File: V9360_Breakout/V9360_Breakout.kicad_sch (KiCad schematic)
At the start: 1 part

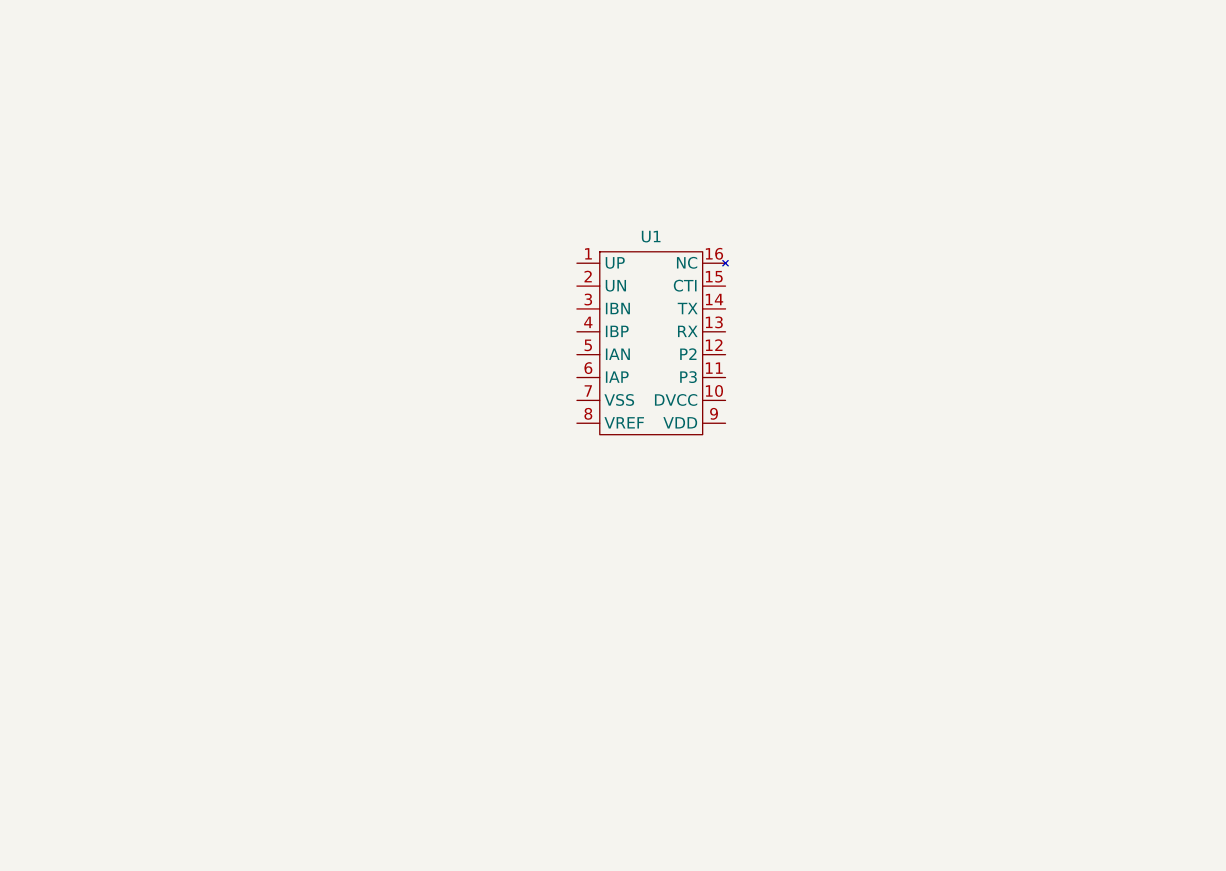
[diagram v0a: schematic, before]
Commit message: Add routing and filters
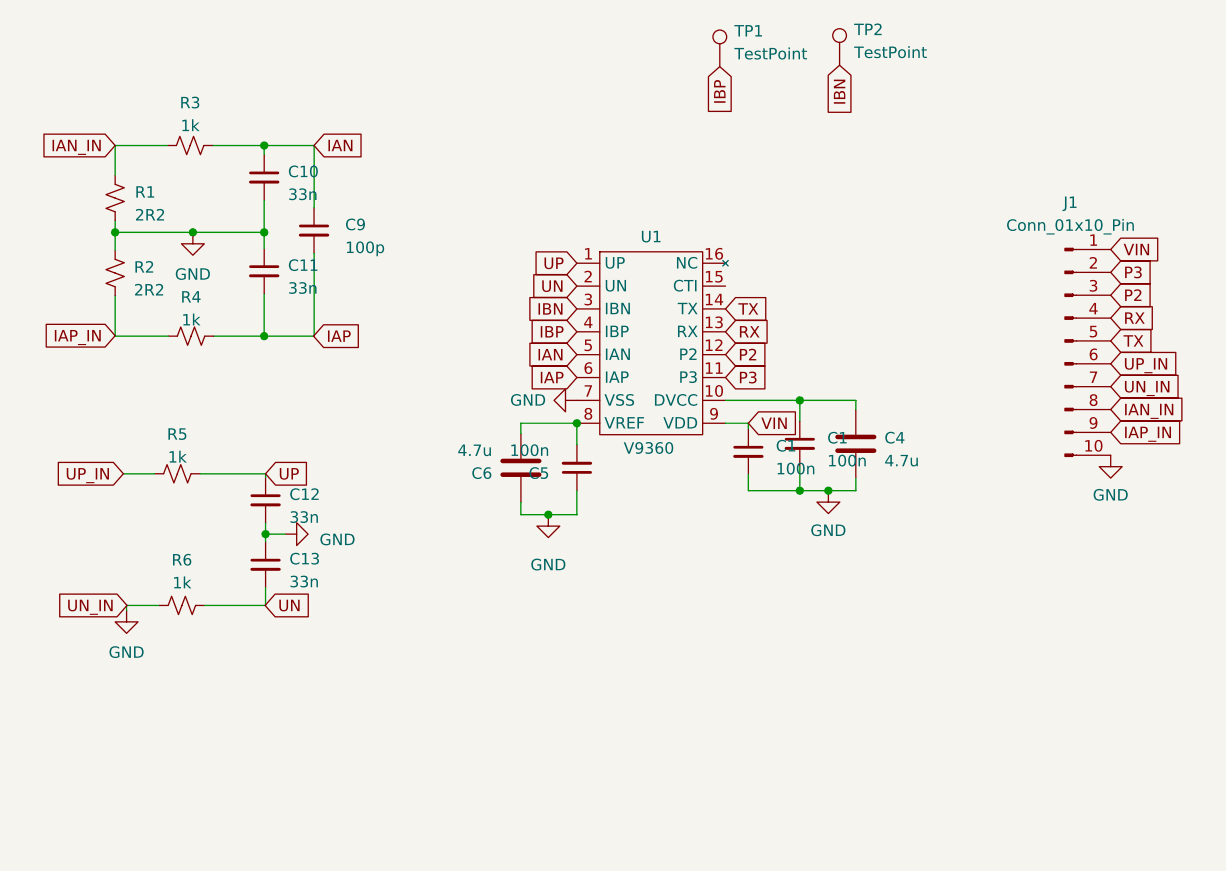
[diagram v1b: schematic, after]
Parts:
- added C1 (x2), C5: 100n, Capacitor_SMD:C_0603_1608Metric, symbol Device:C_Small
- added C10, C11, C12, C13: 33n, Capacitor_SMD:C_0603_1608Metric, symbol Device:C_Small
- added C4, C6: 4.7u, Capacitor_SMD:C_0805_2012Metric, symbol Device:C
- added C9: 100p, Capacitor_SMD:C_0603_1608Metric, symbol Device:C_Small
- added J1: Conn_01x10_Pin, Connector_PinHeader_2.54mm:PinHeader_1x10_P2.54mm_Vertical, symbol Connector:Conn_01x10_Pin
- added R1, R2: 2R2, Resistor_SMD:R_0603_1608Metric, symbol Device:R_Small_US
- added R3, R4, R5, R6: 1k, Resistor_SMD:R_0603_1608Metric, symbol Device:R_Small_US
- added TP1, TP2: TestPoint, TestPoint:TestPoint_Pad_1.5x1.5mm, symbol Connector:TestPoint
- U1: value ~ -> V9360
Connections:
- net UP: now reaches U1.1 (UP)
- net UP: now also C12.1, R5.2
- net at U1.10 (DVCC): now also C1.1, C4.1
- net P3: now reaches U1.11 (P3)
- net P3: now also J1.2 (Pin_2)
- net P2: now reaches U1.12 (P2)
- net P2: now also J1.3 (Pin_3)
- net RX: now reaches U1.13 (RX)
- net RX: now also J1.4 (Pin_4)
- net TX: now reaches U1.14 (TX)
- net TX: now also J1.5 (Pin_5)
- net UN: now reaches U1.2 (UN)
- net UN: now also C13.2, R6.2
- net IBN: now reaches U1.3 (IBN)
- net IBN: now also TP2.1
- net IBP: now reaches U1.4 (IBP)
- net IBP: now also TP1.1
- net IAN: now reaches U1.5 (IAN)
- net IAN: now also C10.1, C9.1, R3.2
- net IAP: now reaches U1.6 (IAP)
- net IAP: now also C11.2, C9.2, R4.2
- net GND: now reaches U1.7 (VSS)
- net GND: now also C1.2, C1.2, C10.2, C11.1, C12.2, C13.1, C4.2, C5.1, C6.1, J1.10 (Pin_10), J1.7 (Pin_7), R1.2, R2.1, R6.1
- net at U1.8 (VREF): now also C5.2, C6.2
- net VIN: now reaches U1.9 (VDD)
- net VIN: now also C1.1, J1.1 (Pin_1)
- new net IAN_IN: J1.8 (Pin_8), R1.1, R3.1
- new net IAP_IN: J1.9 (Pin_9), R2.2, R4.1
- new net UP_IN: J1.6 (Pin_6), R5.1

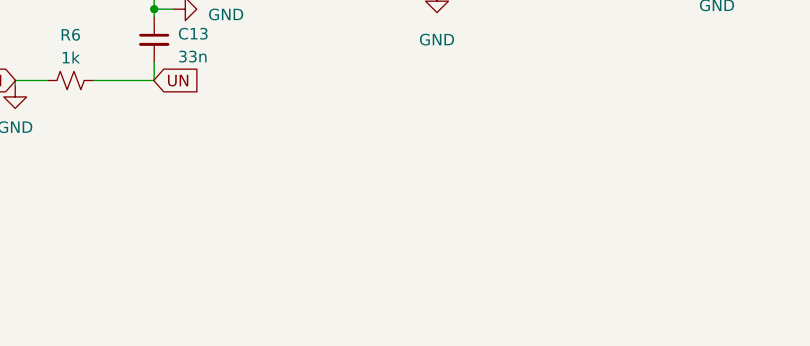
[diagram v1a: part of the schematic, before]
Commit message: Add silk screen refinements
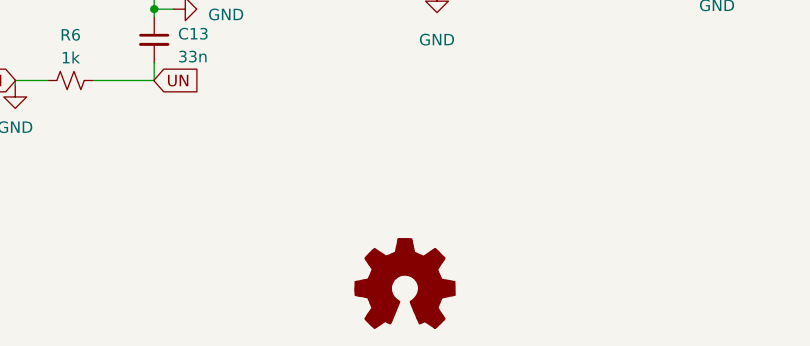
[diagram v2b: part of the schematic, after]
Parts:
- added SYM1: Logo_Open_Hardware_Small, Symbol:OSHW-Logo2_9.8x8mm_SilkScreen, symbol Graphic:Logo_Open_Hardware_Small
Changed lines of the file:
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@@
+    )
+  )
+  (symbol (lib_id "Graphic:Logo_Open_Hardware_Small") (at 125.603 147.955 0) (unit 1)
+    (in_bom no) (on_board yes) (dnp no) (fields_autoplaced)
+    (property "Reference" "SYM1" (at 125.603 140.97 0)
+      (effects (font (size 1.27 1.27)) hide)
+    )
+    (property "Value" "Logo_Open_Hardware_Small" (at 125.603 153.67 0)
+      (effects (font (size 1.27 1.27)) hide)
+    )
+    (property "Footprint" "Symbol:OSHW-Logo2_9.8x8mm_SilkScreen" (at 125.603 147.955 0)
+      (effects (font (size 1.27 1.27)) hide)
+    )
+    (property "Datasheet" "~" (at 125.603 147.955 0)
+      (effects (font (size 1.27 1.27)) hide)
+    )
+    (property "Sim.Enable" "0" (at 125.603 147.955 0)
+      (effects (font (size 1.27 1.27)) hide)
+    )
+    (instances
+      (project "V9360_Breakout"
+        (path "/f6ffeb9c-2174-49f8-b838-c33315c45e1a"
+          (reference "SYM1") (unit 1)
+        )
+      )
     )
   )

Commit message: Add Gerbers and BOM
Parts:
- C1, C5: MPN (none) -> GMC10X7R104K100NT
- C10, C11, C12, C13: MPN (none) -> CC0603JRX7R9BB333
- C4, C6: MPN (none) -> C0805C475K8PACTU
- C9: MPN (none) -> 885012206003
- J1, SYM1, TP1, TP2: DNP (none) -> ...
- R1, R2: MPN (none) -> CPF0603B2R21E1
- R3, R4, R5, R6: MPN (none) -> RR0816P-102-D
- U1: MPN (none) -> V9360
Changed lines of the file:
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@@
+      (effects (font (size 1.27 1.27)) hide)
+    )
+    (property "DNP" "" (at 81.026 87.8332 0)
+      (effects (font (size 1.27 1.27)) hide)
+    )
+    (property "MPN" "CPF0603B2R21E1" (at 81.026 87.8332 0)
       (effects (font (size 1.27 1.27)) hide)
     )
@@
       (effects (font (size 1.27 1.27)) hide)
     )
+    (property "DNP" "" (at 97.7392 120.2436 0)
+      (effects (font (size 1.27 1.27)) hide)
+    )
+    (property "MPN" "CC0603JRX7R9BB333" (at 97.7392 120.2436 0)
+      (effects (font (size 1.27 1.27)) hide)
+    )
     (pin "1")
     (pin "2")
@@
       (effects (font (size 1.27 1.27)) hide)
     )
+    (property "DNP" "" (at 87.9348 110.1344 0)
+      (effects (font (size 1.27 1.27)) hide)
+    )
+    (property "MPN" "RR0816P-102-D" (at 87.9348 110.1344 0)
+      (effects (font (size 1.27 1.27)) hide)
+    )
     (pin "1")
     (pin "2")
@@
       (effects (font (size 1.27 1.27)) hide)
     )
+    (property "DNP" "..." (at 148.209 64.897 0)
+      (effects (font (size 1.27 1.27)) hide)
+    )
+    (property "MPN" "" (at 148.209 64.897 0)
+      (effects (font (size 1.27 1.27)) hide)
+    )
     (pin "1")
     (instances
@@
     )
     (property "Datasheet" "~" (at 97.5868 77.216 0)
+      (effects (font (size 1.27 1.27)) hide)
+    )
+    (property "DNP" "" (at 97.5868 77.216 0)
+      (effects (font (size 1.27 1.27)) hide)
+    )
+    (property "MPN" "CC0603JRX7R9BB333" (at 97.5868 77.216 0)
       (effects (font (size 1.27 1.27)) hide)
     )
@@
       (effects (font (size 1.27 1.27)) hide)
     )
+    (property "DNP" "..." (at 125.603 147.955 0)
+      (effects (font (size 1.27 1.27)) hide)
+    )
+    (property "MPN" "" (at 125.603 147.955 0)
+      (effects (font (size 1.27 1.27)) hide)
+    )
     (instances
       (project "V9360_Breakout"
@@
     )
     (property "Datasheet" "" (at 139.954 84.201 0)
+      (effects (font (size 1.27 1.27)) hide)
+    )
+    (property "DNP" "" (at 139.954 84.201 0)
+      (effects (font (size 1.27 1.27)) hide)
+    )
+    (property "MPN" "V9360" (at 139.954 84.201 0)
       (effects (font (size 1.27 1.27)) hide)
     )
@@
       (effects (font (size 1.27 1.27)) hide)
     )
+    (property "DNP" "" (at 88.4428 124.7648 0)
+      (effects (font (size 1.27 1.27)) hide)
+    )
+    (property "MPN" "RR0816P-102-D" (at 88.4428 124.7648 0)
+      (effects (font (size 1.27 1.27)) hide)
+    )
     (pin "1")
     (pin "2")
@@
     )
     (property "Datasheet" "~" (at 89.4588 94.8436 0)
+      (effects (font (size 1.27 1.27)) hide)
+    )
+    (property "DNP" "" (at 89.4588 94.8436 0)
+      (effects (font (size 1.27 1.27)) hide)
+    )
+    (property "MPN" "RR0816P-102-D" (at 89.4588 94.8436 0)
       (effects (font (size 1.27 1.27)) hide)
     )
@@
       (effects (font (size 1.27 1.27)) hide)
     )
+    (property "DNP" "" (at 163.322 106.807 0)
+      (effects (font (size 1.27 1.27)) hide)
+    )
+    (property "MPN" "C0805C475K8PACTU" (at 163.322 106.807 0)
+      (effects (font (size 1.27 1.27)) hide)
+    )
     (pin "1")
     (pin "2")
@@
       (effects (font (size 1.27 1.27)) hide)
     )
+    (property "DNP" "" (at 126.111 109.474 0)
+      (effects (font (size 1.27 1.27)) hide)
+    )
+    (property "MPN" "C0805C475K8PACTU" (at 126.111 109.474 0)
+      (effects (font (size 1.27 1.27)) hide)
+    )
     (pin "1")
     (pin "2")
@@
       (effects (font (size 1.27 1.27)) hide)
     )
+    (property "DNP" "..." (at 161.5186 64.7446 0)
+      (effects (font (size 1.27 1.27)) hide)
+    )
+    (property "MPN" "" (at 161.5186 64.7446 0)
+      (effects (font (size 1.27 1.27)) hide)
+    )
     (pin "1")
     (instances
@@
       (effects (font (size 1.27 1.27)) hide)
     )
+    (property "DNP" "" (at 157.099 106.807 0)
+      (effects (font (size 1.27 1.27)) hide)
+    )
+    (property "MPN" "GMC10X7R104K100NT" (at 157.099 106.807 0)
+      (effects (font (size 1.27 1.27)) hide)
+    )
     (pin "1")
     (pin "2")
@@
       (effects (font (size 1.27 1.27)) hide)
     )
+    (property "DNP" "" (at 132.334 109.474 0)
+      (effects (font (size 1.27 1.27)) hide)
+    )
+    (property "MPN" "GMC10X7R104K100NT" (at 132.334 109.474 0)
+      (effects (font (size 1.27 1.27)) hide)
+    )
     (pin "1")
     (pin "2")
@@
       (effects (font (size 1.27 1.27)) hide)
     )
+    (property "DNP" "" (at 81.026 79.502 0)
+      (effects (font (size 1.27 1.27)) hide)
+    )
+    (property "MPN" "CPF0603B2R21E1" (at 81.026 79.502 0)
+      (effects (font (size 1.27 1.27)) hide)
+    )
     (pin "1")
     (pin "2")
@@
       (effects (font (size 1.27 1.27)) hide)
     )
+    (property "DNP" "" (at 151.384 107.696 0)
+      (effects (font (size 1.27 1.27)) hide)
+    )
+    (property "MPN" "GMC10X7R104K100NT" (at 151.384 107.696 0)
+      (effects (font (size 1.27 1.27)) hide)
+    )
     (pin "1")
     (pin "2")
@@
       (effects (font (size 1.27 1.27)) hide)
     )
+    (property "DNP" "" (at 89.3572 73.66 0)
+      (effects (font (size 1.27 1.27)) hide)
+    )
+    (property "MPN" "RR0816P-102-D" (at 89.3572 73.66 0)
+      (effects (font (size 1.27 1.27)) hide)
+    )
     (pin "1")
     (pin "2")
@@
     )
     (property "Datasheet" "~" (at 186.563 95.377 0)
+      (effects (font (size 1.27 1.27)) hide)
+    )
+    (property "DNP" "..." (at 186.563 95.377 0)
+      (effects (font (size 1.27 1.27)) hide)
+    )
+    (property "MPN" "" (at 186.563 95.377 0)
       (effects (font (size 1.27 1.27)) hide)
     )
@@
       (effects (font (size 1.27 1.27)) hide)
     )
+    (property "DNP" "" (at 97.5868 87.63 0)
+      (effects (font (size 1.27 1.27)) hide)
+    )
+    (property "MPN" "CC0603JRX7R9BB333" (at 97.5868 87.63 0)
+      (effects (font (size 1.27 1.27)) hide)
+    )
     (pin "1")
     (pin "2")
@@
       (effects (font (size 1.27 1.27)) hide)
     )
+    (property "DNP" "" (at 97.7392 113.0808 0)
+      (effects (font (size 1.27 1.27)) hide)
+    )
+    (property "MPN" "CC0603JRX7R9BB333" (at 97.7392 113.0808 0)
+      (effects (font (size 1.27 1.27)) hide)
+    )
     (pin "1")
     (pin "2")
@@
       (effects (font (size 1.27 1.27)) hide)
     )
+    (property "DNP" "" (at 103.124 83.1088 0)
+      (effects (font (size 1.27 1.27)) hide)
+    )
+    (property "MPN" "885012206003" (at 103.124 83.1088 0)
+      (effects (font (size 1.27 1.27)) hide)
+    )
